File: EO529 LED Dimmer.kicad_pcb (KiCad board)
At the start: 2 copper layers, 73.7 x 58.4 mm, 51 parts, among them J1 VBat, Q1 BC639, Q2 BC639, Q3 BC639, Q4 BC639, U1 NE556, U2 NE556, U3 LM393, U4 LM393

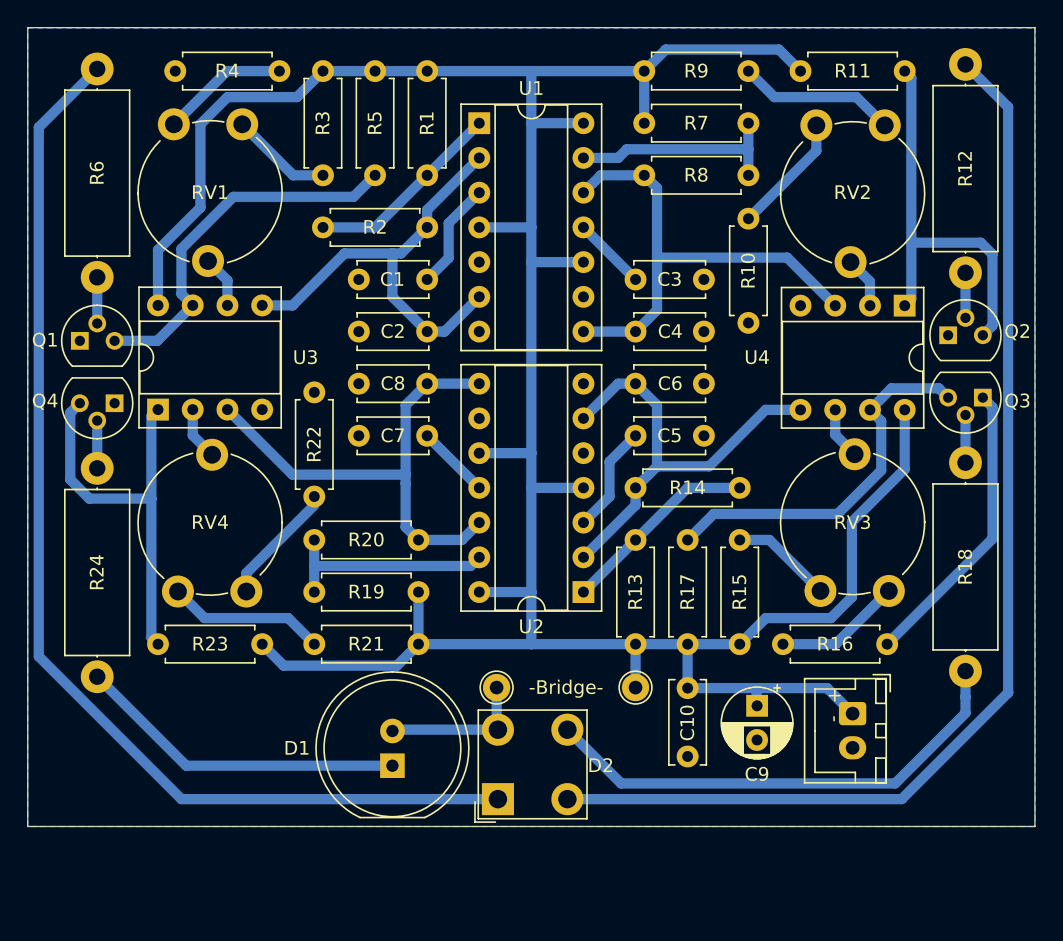
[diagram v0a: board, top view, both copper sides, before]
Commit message: New layout, less parts
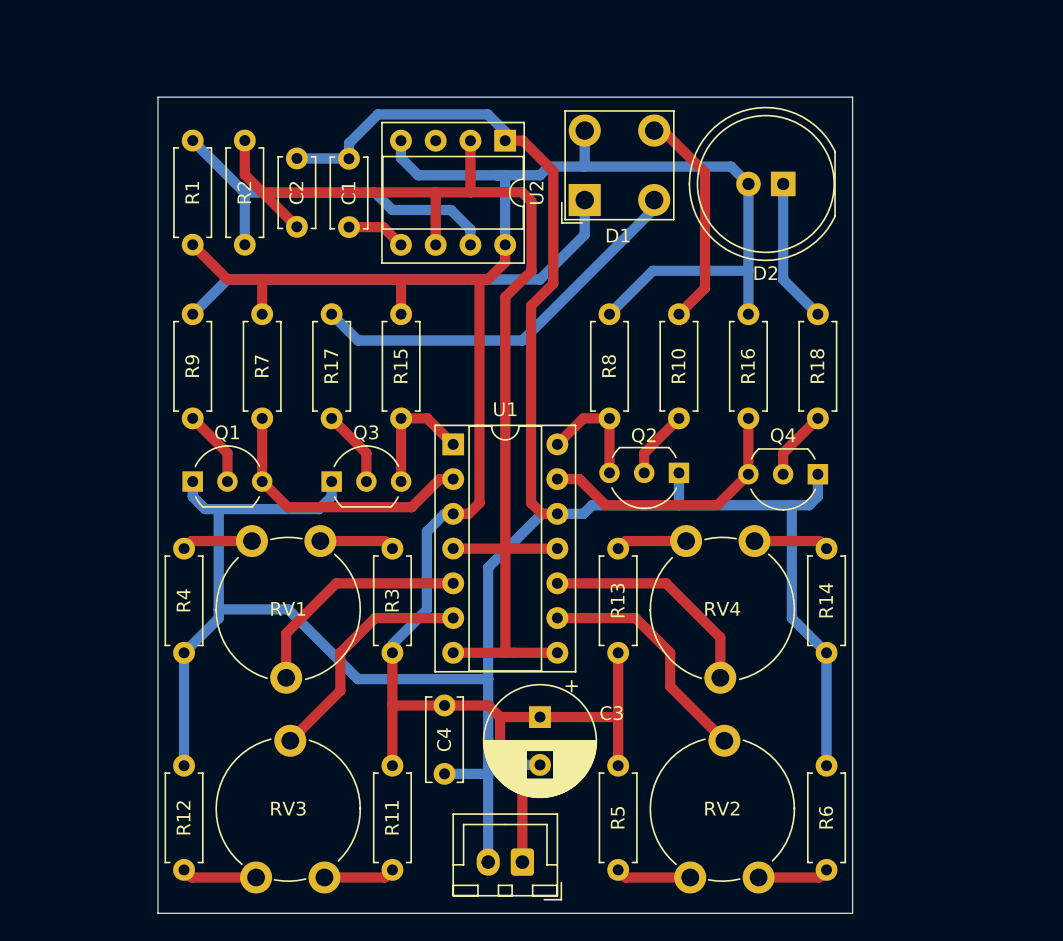
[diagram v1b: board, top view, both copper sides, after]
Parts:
- removed C10: 100n, Capacitor_THT:C_Disc_D6.0mm_W2.5mm_P5.00mm
- removed C5, C6, C7, C8: 10n, Capacitor_THT:C_Disc_D5.0mm_W2.5mm_P5.00mm
- removed C9: 10u, Capacitor_THT:CP_Radial_D5.0mm_P2.50mm
- removed R19, R20: 10k, Resistor_THT:R_Axial_DIN0207_L6.3mm_D2.5mm_P7.62mm_Horizontal
- removed R21, R22: 82k, Resistor_THT:R_Axial_DIN0207_L6.3mm_D2.5mm_P7.62mm_Horizontal
- removed R23: 4.7k, Resistor_THT:R_Axial_DIN0207_L6.3mm_D2.5mm_P7.62mm_Horizontal
- removed R24: 220, Resistor_THT:R_Axial_DIN0414_L11.9mm_D4.5mm_P15.24mm_Horizontal
- removed TP1, TP2: TestPoint, TestPoint:TestPoint_THTPad_D2.0mm_Drill1.0mm
- removed U3, U4: LM393, Package_DIP:DIP-8_W7.62mm_Socket
- C3: value 10n -> 100u; footprint Capacitor_THT:C_Disc_D5.0mm_W2.5mm_P5.00mm -> Capacitor_THT:CP_Radial_D8.0mm_P3.50mm
- C4: value 10n -> 100n; footprint Capacitor_THT:C_Disc_D5.0mm_W2.5mm_P5.00mm -> Capacitor_THT:C_Disc_D6.0mm_W2.5mm_P5.00mm
- D1: value White -> LED_RGBA; footprint LED_THT:LED_D10.0mm -> LED_THT:LED_BL-FL7680RGB
- D2: value LED_RGBA -> White; footprint LED_THT:LED_BL-FL7680RGB -> LED_THT:LED_D10.0mm
- Q1, Q2, Q3, Q4: footprint Package_TO_SOT_THT:TO-92 -> Package_TO_SOT_THT:TO-92_Inline_Wide
- R10: value 82k -> 180
- R11, R5: value 4.7k -> 82k
- R12: value 180 -> 82k; footprint Resistor_THT:R_Axial_DIN0414_L11.9mm_D4.5mm_P15.24mm_Horizontal -> Resistor_THT:R_Axial_DIN0207_L6.3mm_D2.5mm_P7.62mm_Horizontal
- R13, R14: value 10k -> 82k
- R15, R16: value 82k -> 4.7k
- R17: value 4.7k -> 180
- R18: value 180 -> 220; footprint Resistor_THT:R_Axial_DIN0414_L11.9mm_D4.5mm_P15.24mm_Horizontal -> Resistor_THT:R_Axial_DIN0207_L6.3mm_D2.5mm_P7.62mm_Horizontal
- R6: value 150 -> 82k; footprint Resistor_THT:R_Axial_DIN0414_L11.9mm_D4.5mm_P15.24mm_Horizontal -> Resistor_THT:R_Axial_DIN0207_L6.3mm_D2.5mm_P7.62mm_Horizontal
- R7, R8: value 10k -> 4.7k
- R9: value 82k -> 150
- U1: value NE556 -> LM339
- U2: value NE556 -> NE555P; footprint Package_DIP:DIP-14_W7.62mm_Socket -> Package_DIP:DIP-8_W7.62mm_Socket
- moved R12 71.9 mm to (78.1, 130.9)
- moved R6 68.7 mm to (125.1, 130.9)
- moved R11 63.1 mm to (93.3, 123.3), turned to -90 degrees
- moved RV2 55.2 mm to (120.1, 131.4), turned to 90 degrees
- moved Q4 51.7 mm to (124.5, 101.9)
- moved D2 49.6 mm to (121.9, 80.7), turned to 180 degrees
- moved Q3 48.0 mm to (88.9, 102.5), turned to 0 degrees
- moved R5 46.7 mm to (109.9, 123.3), turned to -90 degrees
- moved RV3 46.3 mm to (88.4, 131.4)
- moved D1 43.7 mm to (107.4, 81.9)
- moved R3 42.8 mm to (93.3, 115.0), turned to 90 degrees
- moved R9 41.7 mm to (78.7, 97.9), turned to 90 degrees
- moved R4 35.6 mm to (78.1, 107.4), turned to -90 degrees
- moved R7 35.3 mm to (83.8, 97.9), turned to 90 degrees
- moved U2 33.5 mm to (101.6, 77.5), turned to -90 degrees
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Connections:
- C2 pad 1: Net-(C2-Pad1) -> PWM
- C3 pad 1: Net-(C3-Pad1) -> VCC
- C4 pad 1: Net-(C4-Pad1) -> VCC
- D1 pad 1: Net-(D1-Pad1) -> Red
- D1 pad 2: V_LED -> Green
- D2 pad 1: Red -> Net-(D2-Pad1)
- D2 pad 2: Green -> VCC
- R10 pad 1: Net-(R10-Pad1) -> Net-(Q2-Pad2)
- R10 pad 2: GND -> Blue
- R11 pad 1: Net-(Q2-Pad3) -> VCC
- R11 pad 2: VCC -> Net-(R11-Pad2)
- R12 pad 1: Net-(Q2-Pad2) -> Net-(R12-Pad1)
- R12 pad 2: Green -> GND
- R14 pad 1: Net-(R13-Pad2) -> Net-(R14-Pad1)
- R14 pad 2: Net-(C6-Pad1) -> GND
- R15 pad 1: VCC -> Net-(Q3-Pad3)
- R15 pad 2: Net-(R15-Pad2) -> VCC
- R16 pad 1: Net-(R16-Pad1) -> Net-(Q4-Pad3)
- R16 pad 2: GND -> VCC
- R17 pad 1: Net-(Q3-Pad3) -> Net-(Q3-Pad2)
- R17 pad 2: VCC -> Green
- R18 pad 1: Net-(Q3-Pad2) -> Net-(Q4-Pad2)
- R18 pad 2: Blue -> Net-(D2-Pad1)
- R2 pad 2: Net-(C2-Pad1) -> PWM
- R5 pad 1: Net-(Q1-Pad3) -> VCC
- R5 pad 2: VCC -> Net-(R5-Pad2)
- R6 pad 1: Net-(Q1-Pad2) -> Net-(R6-Pad1)
- R6 pad 2: Red -> GND
- R7 pad 1: VCC -> Net-(Q1-Pad3)
- R7 pad 2: Net-(R7-Pad2) -> VCC
- R8 pad 1: Net-(R7-Pad2) -> Net-(Q2-Pad3)
- R8 pad 2: Net-(C4-Pad1) -> VCC
- R9 pad 1: VCC -> Net-(Q1-Pad2)
- R9 pad 2: Net-(R9-Pad2) -> Red
- RV2 pad 1: Net-(R10-Pad1) -> Net-(R6-Pad1)
- RV2 pad 3: Net-(R9-Pad2) -> Net-(R5-Pad2)
- RV3 pad 1: Net-(R16-Pad1) -> Net-(R11-Pad2)
- RV3 pad 2: Net-(RV3-Pad2) -> Net-(U1-Pad6)
- RV3 pad 3: Net-(R15-Pad2) -> Net-(R12-Pad1)
- RV4 pad 1: Net-(R22-Pad1) -> Net-(R13-Pad2)
- RV4 pad 3: Net-(R21-Pad2) -> Net-(R14-Pad1)
- U1 pad 1: Net-(R1-Pad2) -> Net-(Q3-Pad3)
- U1 pad 10: VCC -> Net-(RV4-Pad2)
- U1 pad 11: Net-(C3-Pad1) -> PWM
- U1 pad 12: Net-(C4-Pad1) -> GND
- U1 pad 13: Net-(R7-Pad2) -> Net-(Q4-Pad3)
- U1 pad 14: VCC -> Net-(Q2-Pad3)
- U1 pad 2: Net-(C2-Pad1) -> Net-(Q1-Pad3)
- U1 pad 3: Net-(C1-Pad1) -> VCC
- U1 pad 4: VCC -> PWM
- U1 pad 5: unconnected-(U1-Pad5) -> Net-(RV1-Pad2)
- U1 pad 6: Net-(C2-Pad1) -> Net-(U1-Pad6)
- U1 pad 7: GND -> PWM
- U1 pad 8: Net-(C4-Pad1) -> PWM
- U1 pad 9: unconnected-(U1-Pad9) -> Net-(RV2-Pad2)
- U2 pad 1: Net-(R13-Pad2) -> GND
- U2 pad 2: Net-(C6-Pad1) -> PWM
- U2 pad 3: Net-(C5-Pad1) -> unconnected-(U2-Pad3)
- U2 pad 5: unconnected-(U2-Pad5) -> Net-(C1-Pad1)
- U2 pad 6: Net-(C6-Pad1) -> PWM
- U2 pad 7: GND -> Net-(R1-Pad2)
- U2 pad 8: Net-(C8-Pad1) -> VCC
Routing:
- net GND: track 21.5 -> 183.7 mm
- net PWM: track 0.00 -> 84.7 mm
- net Green: track 82.7 -> 29.0 mm
- net VCC: track 215.4 -> 163.3 mm
- net Red: track 82.6 -> 33.6 mm
- net Net-(C8-Pad1): track 36.3 -> 0.00 mm
- net Net-(C4-Pad1): track 35.7 -> 0.00 mm
- net Net-(C2-Pad1): track 32.7 -> 0.00 mm
- net Net-(C6-Pad1): track 32.6 -> 0.00 mm
- net Net-(D1-Pad1): track 24.3 -> 0.00 mm
- net Net-(Q2-Pad3): track 30.1 -> 8.58 mm
- net Blue: track 35.9 -> 16.4 mm
- net Net-(Q3-Pad3): track 27.7 -> 9.22 mm
- net Net-(U1-Pad6): track 0.00 -> 17.3 mm
- net Net-(R7-Pad2): track 16.1 -> 0.00 mm
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- removed copper zone on B.Cu, net GND
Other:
- board size 73.7 x 58.4 mm -> 50.8 x 59.7 mm
- board text removed: "- +"
- board text removed: "-Bridge-"

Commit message: Revert "New layout, less parts"
This reverts commit 43836197f3911cfe2976812753205c060315a555.
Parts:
- added C10: 100n, Capacitor_THT:C_Disc_D6.0mm_W2.5mm_P5.00mm, F.Cu at (114.9, 117.6)
- added C5: 10n, Capacitor_THT:C_Disc_D5.0mm_W2.5mm_P5.00mm, F.Cu at (111.1, 99.1)
- added C6: 10n, Capacitor_THT:C_Disc_D5.0mm_W2.5mm_P5.00mm, F.Cu at (111.1, 95.3)
- added C7: 10n, Capacitor_THT:C_Disc_D5.0mm_W2.5mm_P5.00mm, F.Cu at (95.9, 99.1)
- added C8: 10n, Capacitor_THT:C_Disc_D5.0mm_W2.5mm_P5.00mm, F.Cu at (95.9, 95.3)
- added C9: 10u, Capacitor_THT:CP_Radial_D5.0mm_P2.50mm, F.Cu at (120.0, 118.9)
- added R19: 10k, Resistor_THT:R_Axial_DIN0207_L6.3mm_D2.5mm_P7.62mm_Horizontal, F.Cu at (95.2, 110.6)
- added R20: 10k, Resistor_THT:R_Axial_DIN0207_L6.3mm_D2.5mm_P7.62mm_Horizontal, F.Cu at (87.6, 106.7)
- added R21: 82k, Resistor_THT:R_Axial_DIN0207_L6.3mm_D2.5mm_P7.62mm_Horizontal, F.Cu at (95.2, 114.4)
- added R22: 82k, Resistor_THT:R_Axial_DIN0207_L6.3mm_D2.5mm_P7.62mm_Horizontal, F.Cu at (87.6, 103.6)
- added R23: 4.7k, Resistor_THT:R_Axial_DIN0207_L6.3mm_D2.5mm_P7.62mm_Horizontal, F.Cu at (76.2, 114.4)
- added R24: 220, Resistor_THT:R_Axial_DIN0414_L11.9mm_D4.5mm_P15.24mm_Horizontal, F.Cu at (71.8, 101.5)
- added TP1: TestPoint, TestPoint:TestPoint_THTPad_D2.0mm_Drill1.0mm, F.Cu at (101.0, 117.5)
- added TP2: TestPoint, TestPoint:TestPoint_THTPad_D2.0mm_Drill1.0mm, F.Cu at (111.1, 117.5)
- added U3: LM393, Package_DIP:DIP-8_W7.62mm_Socket, F.Cu at (76.2, 97.2)
- added U4: LM393, Package_DIP:DIP-8_W7.62mm_Socket, F.Cu at (130.8, 89.6)
- C3: value 100u -> 10n; footprint Capacitor_THT:CP_Radial_D8.0mm_P3.50mm -> Capacitor_THT:C_Disc_D5.0mm_W2.5mm_P5.00mm
- C4: value 100n -> 10n; footprint Capacitor_THT:C_Disc_D6.0mm_W2.5mm_P5.00mm -> Capacitor_THT:C_Disc_D5.0mm_W2.5mm_P5.00mm
- D1: value LED_RGBA -> White; footprint LED_THT:LED_BL-FL7680RGB -> LED_THT:LED_D10.0mm
- D2: value White -> LED_RGBA; footprint LED_THT:LED_D10.0mm -> LED_THT:LED_BL-FL7680RGB
- Q1, Q2, Q3, Q4: footprint Package_TO_SOT_THT:TO-92_Inline_Wide -> Package_TO_SOT_THT:TO-92
- R10: value 180 -> 82k
- R11, R5: value 82k -> 4.7k
- R12: value 82k -> 180; footprint Resistor_THT:R_Axial_DIN0207_L6.3mm_D2.5mm_P7.62mm_Horizontal -> Resistor_THT:R_Axial_DIN0414_L11.9mm_D4.5mm_P15.24mm_Horizontal
- R13, R14: value 82k -> 10k
- R15, R16: value 4.7k -> 82k
- R17: value 180 -> 4.7k
- R18: value 220 -> 180; footprint Resistor_THT:R_Axial_DIN0207_L6.3mm_D2.5mm_P7.62mm_Horizontal -> Resistor_THT:R_Axial_DIN0414_L11.9mm_D4.5mm_P15.24mm_Horizontal
- R6: value 82k -> 150; footprint Resistor_THT:R_Axial_DIN0207_L6.3mm_D2.5mm_P7.62mm_Horizontal -> Resistor_THT:R_Axial_DIN0414_L11.9mm_D4.5mm_P15.24mm_Horizontal
- R7, R8: value 4.7k -> 10k
- R9: value 150 -> 82k
- U1: value LM339 -> NE556
- U2: value NE555P -> NE556; footprint Package_DIP:DIP-8_W7.62mm_Socket -> Package_DIP:DIP-14_W7.62mm_Socket
- moved R12 71.9 mm to (135.3, 87.2)
- moved R6 68.7 mm to (71.8, 87.5)
- moved R11 63.1 mm to (130.8, 72.5), turned to 180 degrees
- moved RV2 55.2 mm to (124.3, 76.4), turned to -90 degrees
- moved Q4 51.7 mm to (73.0, 96.7)
- moved D2 49.6 mm to (101.1, 125.7), turned to 90 degrees
- moved Q3 48.0 mm to (136.5, 96.3), turned to 180 degrees
- moved R5 46.7 mm to (92.1, 80.1), turned to 90 degrees
- moved RV3 46.3 mm to (129.6, 110.5)
- moved D1 43.7 mm to (93.3, 123.3)
- moved R3 42.8 mm to (88.3, 72.5), turned to -90 degrees
- moved R9 41.7 mm to (111.8, 72.5), turned to 0 degrees
- moved R4 35.6 mm to (85.1, 72.5), turned to 180 degrees
- moved R7 35.3 mm to (111.8, 76.3), turned to 0 degrees
- moved U2 33.5 mm to (107.3, 110.6), turned to 180 degrees
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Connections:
- C2 pad 1: PWM -> Net-(C2-Pad1)
- C3 pad 1: VCC -> Net-(C3-Pad1)
- C4 pad 1: VCC -> Net-(C4-Pad1)
- D1 pad 1: Red -> Net-(D1-Pad1)
- D1 pad 2: Green -> V_LED
- D2 pad 1: Net-(D2-Pad1) -> Red
- D2 pad 2: VCC -> Green
- R10 pad 1: Net-(Q2-Pad2) -> Net-(R10-Pad1)
- R10 pad 2: Blue -> GND
- R11 pad 1: VCC -> Net-(Q2-Pad3)
- R11 pad 2: Net-(R11-Pad2) -> VCC
- R12 pad 1: Net-(R12-Pad1) -> Net-(Q2-Pad2)
- R12 pad 2: GND -> Green
- R14 pad 1: Net-(R14-Pad1) -> Net-(R13-Pad2)
- R14 pad 2: GND -> Net-(C6-Pad1)
- R15 pad 1: Net-(Q3-Pad3) -> VCC
- R15 pad 2: VCC -> Net-(R15-Pad2)
- R16 pad 1: Net-(Q4-Pad3) -> Net-(R16-Pad1)
- R16 pad 2: VCC -> GND
- R17 pad 1: Net-(Q3-Pad2) -> Net-(Q3-Pad3)
- R17 pad 2: Green -> VCC
- R18 pad 1: Net-(Q4-Pad2) -> Net-(Q3-Pad2)
- R18 pad 2: Net-(D2-Pad1) -> Blue
- R2 pad 2: PWM -> Net-(C2-Pad1)
- R5 pad 1: VCC -> Net-(Q1-Pad3)
- R5 pad 2: Net-(R5-Pad2) -> VCC
- R6 pad 1: Net-(R6-Pad1) -> Net-(Q1-Pad2)
- R6 pad 2: GND -> Red
- R7 pad 1: Net-(Q1-Pad3) -> VCC
- R7 pad 2: VCC -> Net-(R7-Pad2)
- R8 pad 1: Net-(Q2-Pad3) -> Net-(R7-Pad2)
- R8 pad 2: VCC -> Net-(C4-Pad1)
- R9 pad 1: Net-(Q1-Pad2) -> VCC
- R9 pad 2: Red -> Net-(R9-Pad2)
- RV2 pad 1: Net-(R6-Pad1) -> Net-(R10-Pad1)
- RV2 pad 3: Net-(R5-Pad2) -> Net-(R9-Pad2)
- RV3 pad 1: Net-(R11-Pad2) -> Net-(R16-Pad1)
- RV3 pad 2: Net-(U1-Pad6) -> Net-(RV3-Pad2)
- RV3 pad 3: Net-(R12-Pad1) -> Net-(R15-Pad2)
- RV4 pad 1: Net-(R13-Pad2) -> Net-(R22-Pad1)
- RV4 pad 3: Net-(R14-Pad1) -> Net-(R21-Pad2)
- U1 pad 1: Net-(Q3-Pad3) -> Net-(R1-Pad2)
- U1 pad 10: Net-(RV4-Pad2) -> VCC
- U1 pad 11: PWM -> Net-(C3-Pad1)
- U1 pad 12: GND -> Net-(C4-Pad1)
- U1 pad 13: Net-(Q4-Pad3) -> Net-(R7-Pad2)
- U1 pad 14: Net-(Q2-Pad3) -> VCC
- U1 pad 2: Net-(Q1-Pad3) -> Net-(C2-Pad1)
- U1 pad 3: VCC -> Net-(C1-Pad1)
- U1 pad 4: PWM -> VCC
- U1 pad 5: Net-(RV1-Pad2) -> unconnected-(U1-Pad5)
- U1 pad 6: Net-(U1-Pad6) -> Net-(C2-Pad1)
- U1 pad 7: PWM -> GND
- U1 pad 8: PWM -> Net-(C4-Pad1)
- U1 pad 9: Net-(RV2-Pad2) -> unconnected-(U1-Pad9)
- U2 pad 1: GND -> Net-(R13-Pad2)
- U2 pad 2: PWM -> Net-(C6-Pad1)
- U2 pad 3: unconnected-(U2-Pad3) -> Net-(C5-Pad1)
- U2 pad 5: Net-(C1-Pad1) -> unconnected-(U2-Pad5)
- U2 pad 6: PWM -> Net-(C6-Pad1)
- U2 pad 7: Net-(R1-Pad2) -> GND
- U2 pad 8: VCC -> Net-(C8-Pad1)
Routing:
- net GND: track 183.7 -> 21.5 mm
- net PWM: track 84.7 -> 0.00 mm
- net Green: track 29.0 -> 82.7 mm
- net VCC: track 163.3 -> 215.4 mm
- net Red: track 33.6 -> 82.6 mm
- net Net-(C8-Pad1): track 0.00 -> 36.3 mm
- net Net-(C4-Pad1): track 0.00 -> 35.7 mm
- net Net-(C2-Pad1): track 0.00 -> 32.7 mm
- net Net-(C6-Pad1): track 0.00 -> 32.6 mm
- net Net-(D1-Pad1): track 0.00 -> 24.3 mm
- net Net-(Q2-Pad3): track 8.58 -> 30.1 mm
- net Blue: track 16.4 -> 35.9 mm
- net Net-(Q3-Pad3): track 9.22 -> 27.7 mm
- net Net-(U1-Pad6): track 17.3 -> 0.00 mm
- net Net-(R7-Pad2): track 0.00 -> 16.1 mm
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- added copper zone on B.Cu, net GND
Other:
- board size 50.8 x 59.7 mm -> 73.7 x 58.4 mm
- board text added: "- +"
- board text added: "-Bridge-"
